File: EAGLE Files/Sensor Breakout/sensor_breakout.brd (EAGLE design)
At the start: 100 x 80 mm, 8 parts, among them U1 BMP180

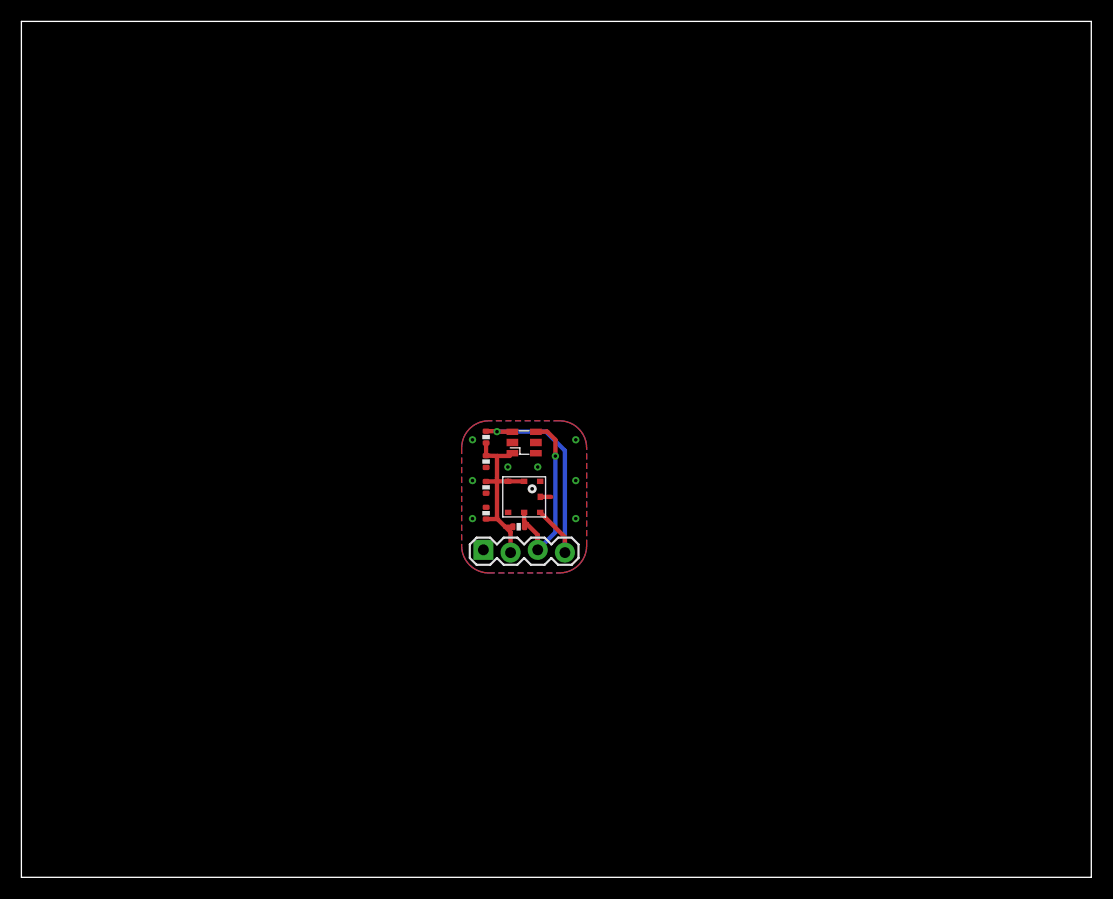
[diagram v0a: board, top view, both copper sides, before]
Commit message: Forgot to adjust physical outline of the board. Fixed and board is now really uploaded to CircuitGraphics.
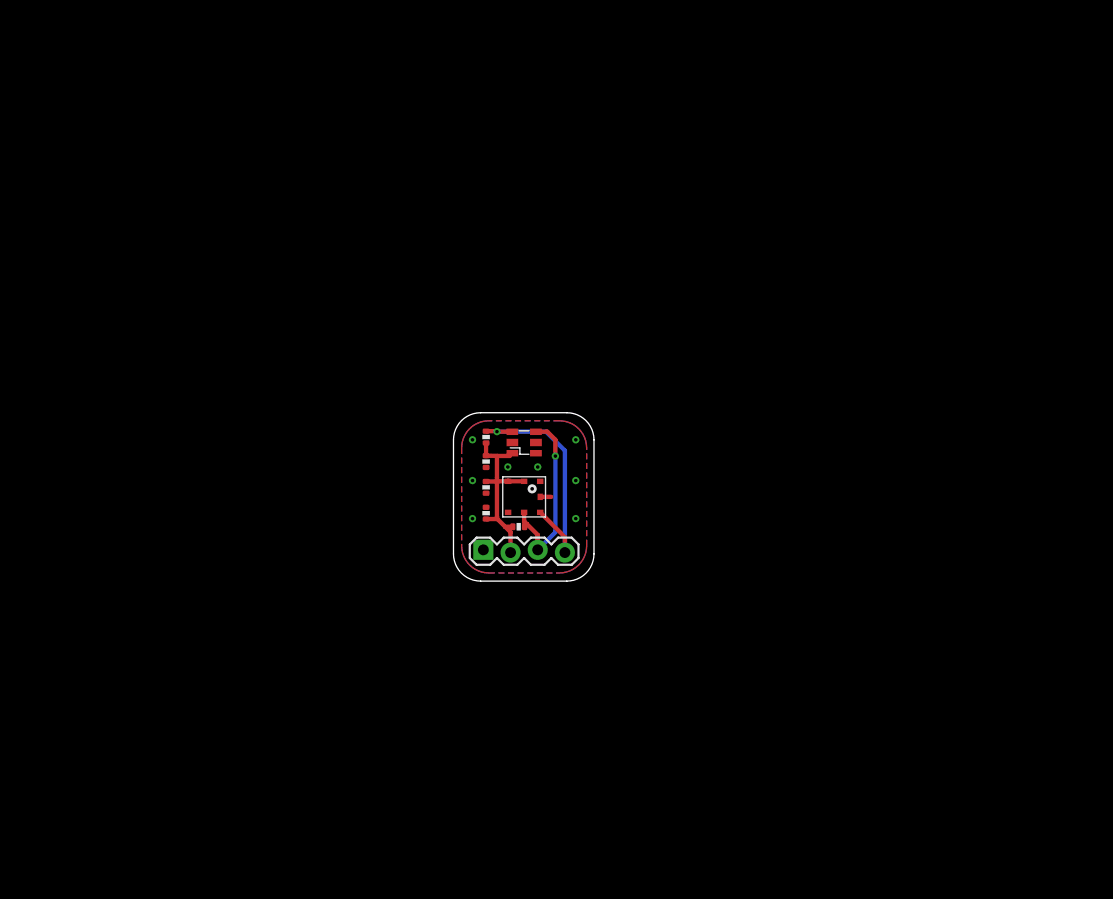
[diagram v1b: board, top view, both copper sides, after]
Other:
- board size 100 x 80 mm -> 13.1 x 15.7 mm
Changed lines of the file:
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@@
 <board>
 <plain>
-<wire x1="0" y1="0" x2="100" y2="0" width="0" layer="20"/>
-<wire x1="100" y1="0" x2="100" y2="80" width="0" layer="20"/>
-<wire x1="100" y1="80" x2="0" y2="80" width="0" layer="20"/>
-<wire x1="0" y1="80" x2="0" y2="0" width="0" layer="20"/>
+<wire x1="40.386" y1="40.884" x2="40.386" y2="30.226" width="0" layer="20"/>
+<wire x1="40.386" y1="30.226" x2="42.926" y2="27.686" width="0" layer="20" curve="90"/>
+<wire x1="42.926" y1="27.686" x2="50.978" y2="27.686" width="0" layer="20"/>
+<wire x1="50.978" y1="27.686" x2="53.518" y2="30.226" width="0" layer="20" curve="90"/>
+<wire x1="53.518" y1="30.226" x2="53.518" y2="40.884" width="0" layer="20"/>
+<wire x1="53.518" y1="40.884" x2="50.978" y2="43.424" width="0" layer="20" curve="90"/>
+<wire x1="50.978" y1="43.424" x2="42.926" y2="43.424" width="0" layer="20"/>
+<wire x1="42.926" y1="43.424" x2="40.386" y2="40.884" width="0" layer="20" curve="90"/>
 <wire x1="46.228" y1="33.528" x2="46.228" y2="34.798" width="0.254" layer="41"/>
 <wire x1="46.228" y1="34.798" x2="47.752" y2="34.798" width="0.254" layer="41"/>
